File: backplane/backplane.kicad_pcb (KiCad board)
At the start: 2 copper layers, 218.4 x 132.1 mm, 96 parts, among them J1 C96ABC, J10 C96ABC, J11 C96ABC, J12 C96ABC, J2 C96ABC, J3 C96ABC, J4 C96ABC, J5 C96ABC, J6 C96ABC, J7 C96ABC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

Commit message: routed backplane
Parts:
- added G***: LOGO, common:logo, B.Cu at (198.1, 33.3)
- added G***: LOGO, common:logo, F.Cu at (111.8, 33.3)
- added JP1: Jumper, Connector_PinHeader_2.54mm:PinHeader_1x02_P2.54mm_Vertical, B.Cu at (68.6, 75.2)
- added JP10: Jumper, Connector_PinHeader_2.54mm:PinHeader_1x02_P2.54mm_Vertical, B.Cu at (251.5, 75.2)
- added JP2: Jumper, Connector_PinHeader_2.54mm:PinHeader_1x02_P2.54mm_Vertical, B.Cu at (88.9, 75.2)
- added JP3: Jumper, Connector_PinHeader_2.54mm:PinHeader_1x02_P2.54mm_Vertical, B.Cu at (109.2, 75.2)
- added JP4: Jumper, Connector_PinHeader_2.54mm:PinHeader_1x02_P2.54mm_Vertical, B.Cu at (129.5, 75.2)
- added JP5: Jumper, Connector_PinHeader_2.54mm:PinHeader_1x02_P2.54mm_Vertical, B.Cu at (149.9, 75.2)
- added JP6: Jumper, Connector_PinHeader_2.54mm:PinHeader_1x02_P2.54mm_Vertical, B.Cu at (170.2, 75.2)
- added JP7: Jumper, Connector_PinHeader_2.54mm:PinHeader_1x02_P2.54mm_Vertical, B.Cu at (190.5, 75.2)
- added JP8: Jumper, Connector_PinHeader_2.54mm:PinHeader_1x02_P2.54mm_Vertical, B.Cu at (210.8, 75.2)
- added JP9: Jumper, Connector_PinHeader_2.54mm:PinHeader_1x02_P2.54mm_Vertical, B.Cu at (231.1, 75.2)
- J11, J12: value C96ABC -> Conn_02x32_Odd_Even; footprint common:Socket_DIN41612-CaseC1-full-Male-96Pin-3rows -> Connector_IDC:IDC-Header_2x32_P2.54mm_Vertical
- moved J12 223.2 mm to (260.4, 47.3), turned to 180 degrees
- moved J11 220.7 mm to (52.1, 47.3), turned to 180 degrees
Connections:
- J11 pad 1: (no net) -> VCC
- J12 pad 1: (no net) -> VCC
- REF** pad 1: (no net) -> GND (x84)
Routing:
- net RESB: track 0.00 -> 261.6 mm
- net VCC: track 0.00 -> 250.5 mm
- net +12V: track 0.00 -> 240.5 mm
- net ~WR: track 0.00 -> 222.0 mm
- net ~NMI: track 0.00 -> 222.0 mm
- net ~M1: track 0.00 -> 222.0 mm
- net ~BUSAK: track 0.00 -> 222.0 mm
- net CLK: track 0.00 -> 222.0 mm
- net A7: track 0.00 -> 222.0 mm
- net A6: track 0.00 -> 222.0 mm
- net A13: track 0.00 -> 222.0 mm
- net ~RESET: track 0.00 -> 222.0 mm
- net D5: track 0.00 -> 222.0 mm
- net A2: track 0.00 -> 222.0 mm
- net D6: track 0.00 -> 222.0 mm
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- added copper zone on B.Cu, net GND
- added copper zone on F.Cu, net GND
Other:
- net class Default: trace_width 0.25 -> 0.4; via_dia 0.8 -> 0.6; via_drill 0.4 -> 0.3
- net class POWER added: clearance 0.2, trace_width 0.6, via_dia 0.8, via_drill 0.4
- board text added: "Micro21 ECB Backplane (42 HP)"

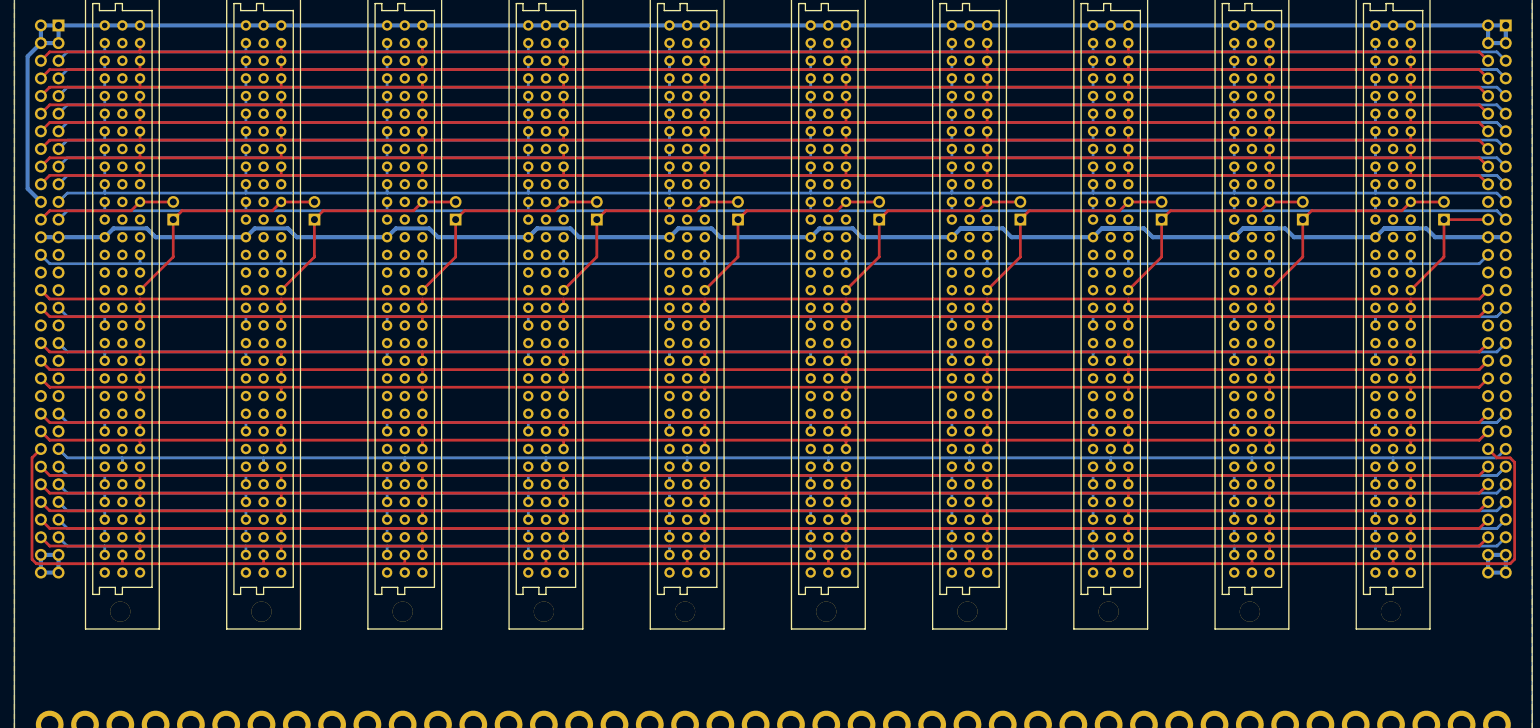
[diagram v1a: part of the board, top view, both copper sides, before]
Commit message: add reset button, minor tweaks
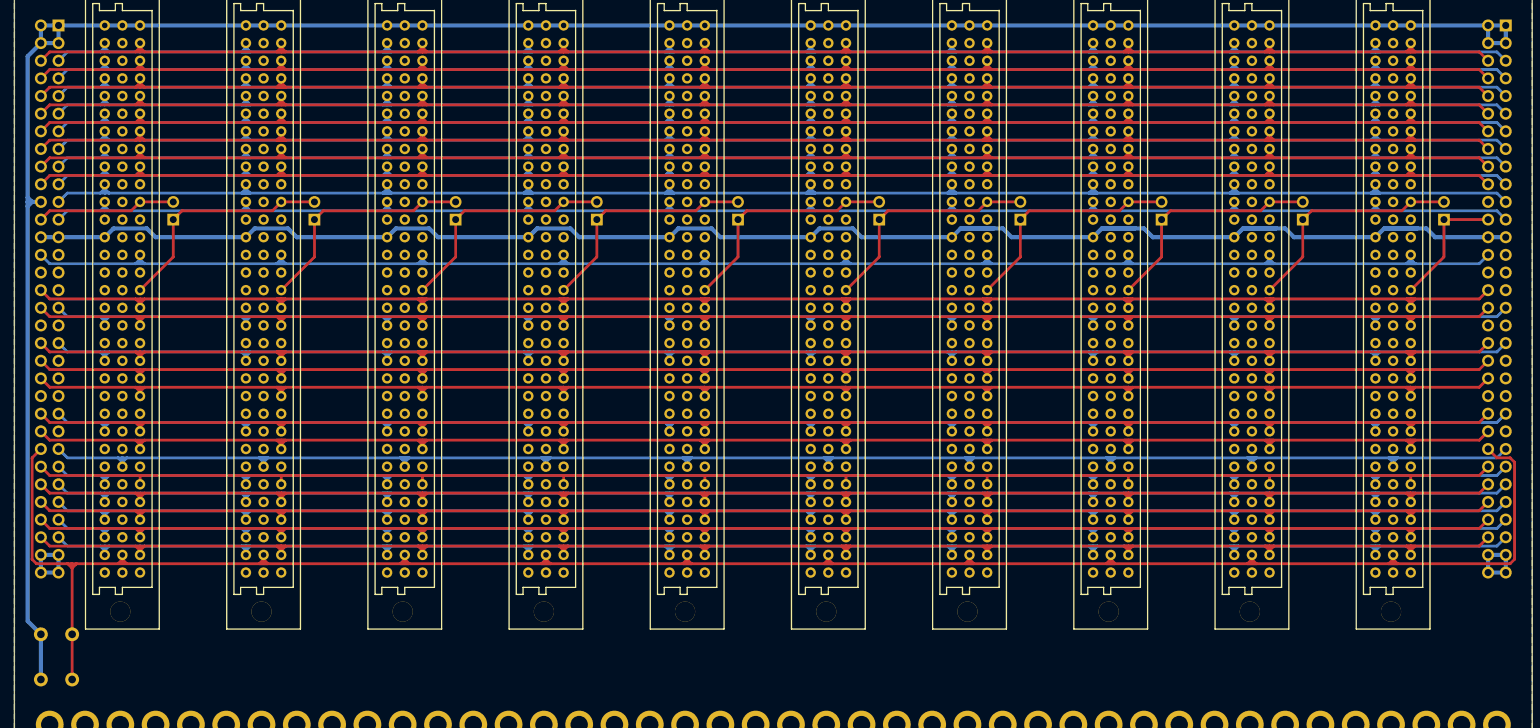
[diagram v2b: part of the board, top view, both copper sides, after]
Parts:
- added SW1: SW_Push, Button_Switch_THT:SW_PUSH_6mm_H7.3mm, B.Cu at (49.5, 134.9)
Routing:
- net VCC: track 250.5 -> 322.9 mm
- net RESB: track 261.6 -> 320.9 mm
- net ~RESET: track 222.0 -> 262.9 mm
- net ~NMI: track 222.0 -> 262.9 mm
- net ~M1: track 222.0 -> 262.9 mm
- net ~BUSAK: track 222.0 -> 262.9 mm
- net CLK: track 222.0 -> 262.9 mm
- net A7: track 222.0 -> 262.9 mm
- net A13: track 222.0 -> 262.9 mm
- net ~MREQ: track 222.0 -> 262.9 mm
- net ~HALT: track 222.0 -> 262.9 mm
- net A9: track 222.0 -> 262.9 mm
- net A14: track 222.0 -> 262.9 mm
- net ~RFSH: track 222.0 -> 262.9 mm
- net ~RD: track 222.0 -> 262.9 mm
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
